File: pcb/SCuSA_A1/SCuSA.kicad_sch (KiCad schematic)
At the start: 37 parts, among them J102 USB4135-GF-A, J105 JST_S2B-PH-K-x, Q102 DMN2041LSD, SW101 SW_DPDT_x2, SW102 SW_SPST, U1 LM27762, U101 MCP73812T-420I-OT, U102 AD8418, U103 BQ297xy, U104 TLV803EA30DBZR

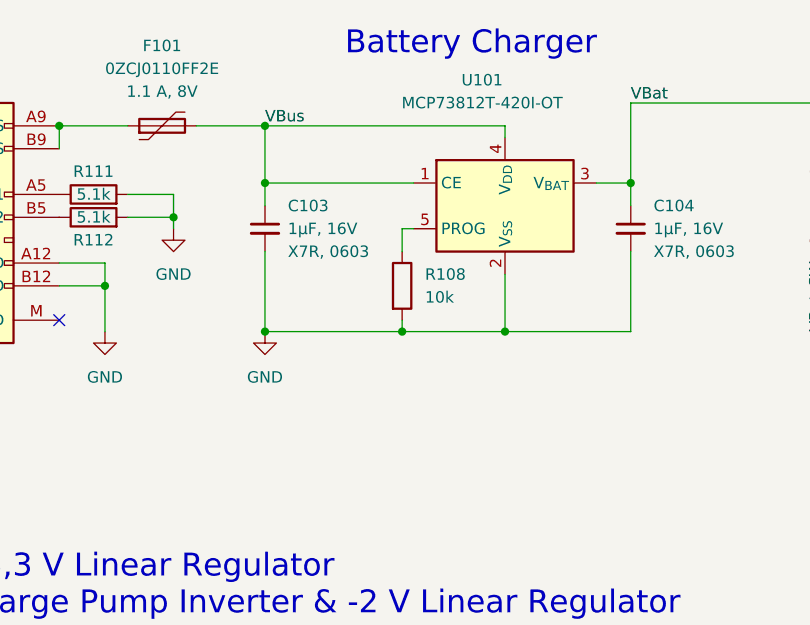
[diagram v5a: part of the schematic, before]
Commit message: Change battery charger
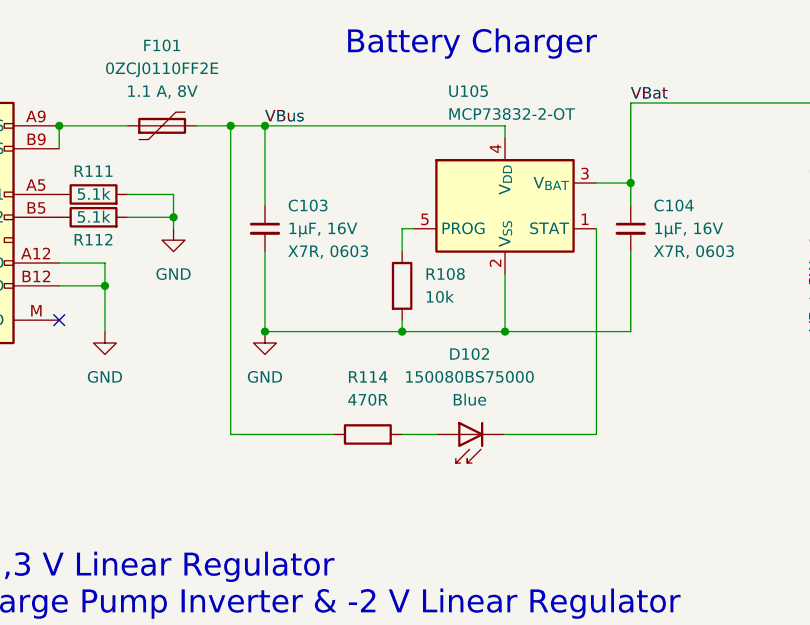
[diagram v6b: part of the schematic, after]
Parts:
- removed U101: MCP73812T-420I-OT, Package_TO_SOT_SMD:SOT-23-5, symbol Battery_Management:MCP73812T-420I-OT
- added D102: 150080BS75000, LED_SMD:LED_0805_2012Metric_Pad1.15x1.40mm_HandSolder, symbol LED_User:150080BS75000
- added R114: 470R,0603, Resistor_SMD:R_0603_1608Metric_Pad0.98x0.95mm_HandSolder, symbol Resistor_User:470R,0603
- added U105: MCP73832-2-OT, Package_TO_SOT_SMD:SOT-23-5, symbol Battery_Management:MCP73832-2-OT
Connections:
- net GND: now also U105.2 (V_{SS})
- net VBat: now also U105.3 (V_{BAT})
- net VBus: now also R114.1, U105.4 (V_{DD})
- net at R108.1: now also U105.5 (PROG)
- new net: D102.2 (A), R114.2
- new net: D102.1 (K), U105.1 (STAT)
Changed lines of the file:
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@@
   (junction (at 52.07 45.72) (diameter 0) (color 0 0 0 0)
   )
-  (junction (at 69.85 34.29) (diameter 0) (color 0 0 0 0)
-  )
   (junction (at 96.52 50.8) (diameter 0) (color 0 0 0 0)
   )
@@
   )
   (junction (at 236.22 27.94) (diameter 0) (color 0 0 0 0)
+  )
+  (junction (at 66.04 27.94) (diameter 0) (color 0 0 0 0)
   )
   (no_connect (at 46.99 49.53))
@@
     (stroke (width 0) (type default))
   )
-  (wire (pts (xy 69.85 36.83) (xy 69.85 34.29))
+  (wire (pts (xy 69.85 27.94) (xy 69.85 36.83))
     (stroke (width 0) (type default))
   )
@@
     (stroke (width 0) (type default))
   )
+  (wire (pts (xy 106.68 62.23) (xy 96.52 62.23))
+    (stroke (width 0) (type default))
+  )
   (wire (pts (xy 171.45 91.44) (xy 171.45 93.98))
     (stroke (width 0) (type default))
@@
     (stroke (width 0) (type default))
   )
-  (wire (pts (xy 96.52 29.21) (xy 96.52 27.94))
-    (stroke (width 0) (type default))
-  )
   (wire (pts (xy 236.22 41.91) (xy 236.22 38.1))
     (stroke (width 0) (type default))
@@
     (stroke (width 0) (type default))
   )
-  (wire (pts (xy 69.85 27.94) (xy 69.85 34.29))
-    (stroke (width 0) (type default))
-  )
   (wire (pts (xy 48.26 113.03) (xy 57.15 113.03))
     (stroke (width 0) (type default))
@@
     (stroke (width 0) (type default))
   )
+  (wire (pts (xy 106.68 39.37) (xy 106.68 62.23))
+    (stroke (width 0) (type default))
+  )
   (wire (pts (xy 251.46 52.07) (xy 236.22 52.07))
     (stroke (width 0) (type default))
@@
     (stroke (width 0) (type default))
   )
+  (wire (pts (xy 66.04 27.94) (xy 69.85 27.94))
+    (stroke (width 0) (type default))
+  )
   (wire (pts (xy 241.3 113.03) (xy 241.3 135.89))
     (stroke (width 0) (type default))
@@
     (stroke (width 0) (type default))
   )
+  (wire (pts (xy 96.52 27.94) (xy 96.52 29.21))
+    (stroke (width 0) (type default))
+  )
   (wire (pts (xy 69.85 50.8) (xy 85.09 50.8))
     (stroke (width 0) (type default))
@@
     (stroke (width 0) (type default))
   )
-  (wire (pts (xy 62.23 27.94) (xy 69.85 27.94))
+  (wire (pts (xy 62.23 27.94) (xy 66.04 27.94))
     (stroke (width 0) (type default))
   )
@@
     (stroke (width 0) (type default))
   )
+  (wire (pts (xy 66.04 62.23) (xy 66.04 27.94))
+    (stroke (width 0) (type default))
+  )
   (wire (pts (xy 190.5 43.18) (xy 190.5 44.45))
     (stroke (width 0) (type default))
@@
     (stroke (width 0) (type default))
   )
+  (wire (pts (xy 77.47 62.23) (xy 66.04 62.23))
+    (stroke (width 0) (type default))
+  )
   (wire (pts (xy 251.46 30.48) (xy 251.46 52.07))
     (stroke (width 0) (type default))
@@
     (stroke (width 0) (type default))
   )
-  (wire (pts (xy 69.85 34.29) (xy 86.36 34.29))
-    (stroke (width 0) (type default))
-  )
   (wire (pts (xy 90.17 135.89) (xy 90.17 138.43))
     (stroke (width 0) (type default))
   )
   (wire (pts (xy 106.68 34.29) (xy 110.49 34.29))
+    (stroke (width 0) (type default))
+  )
+  (wire (pts (xy 88.9 62.23) (xy 85.09 62.23))
     (stroke (width 0) (type default))
   )
@@
     )
   )
-  (symbol (lib_id "Battery_Management:MCP73812T-420I-OT") (at 96.52 36.83 0) (unit 1)
-    (in_bom yes) (on_board yes) (dnp no)
-    (property "Reference" "U101" (at 93.98 22.86 0)
-      (effects (font (size 1.27 1.27)))
-    )
-    (property "Value" "MCP73812T-420I-OT" (at 93.98 25.4 0)
-      (effects (font (size 1.27 1.27)))
-    )
-    (property "Footprint" "Package_TO_SOT_SMD:SOT-23-5" (at 97.79 43.18 0)
-      (effects (font (size 1.27 1.27)) (justify left) hide)
-    )
-    (property "Datasheet" "http://ww1.microchip.com/downloads/en/DeviceDoc/22036b.pdf" (at 90.17 30.48 0)
-      (effects (font (size 1.27 1.27)) hide)
-    )
-    (pin "1")
-    (pin "2")
-    (pin "3")
-    (pin "4")
-    (pin "5")
-    (instances
-      (project "SCuSA"
-        (path "/7c524ebf-103a-4dc7-9ca9-e5a941b364b9"
-          (reference "U101") (unit 1)
-        )
-      )
-    )
-  )
   (symbol (lib_id "Switch:SW_DPDT_x2") (at 241.3 140.97 270) (unit 2)
     (in_bom yes) (on_board yes) (dnp no) (fields_autoplaced)
@@
         (path "/7c524ebf-103a-4dc7-9ca9-e5a941b364b9"
           (reference "JP102") (unit 1)
+        )
+      )
+    )
+  )
+  (symbol (lib_id "Resistor_User:470R,0603") (at 81.28 62.23 90) (unit 1)
+    (in_bom yes) (on_board yes) (dnp no) (fields_autoplaced)
+    (property "Reference" "R114" (at 81.28 55.88 90)
+      (effects (font (size 1.27 1.27)))
+    )
+    (property "Value" "470R,0603" (at 78.74 60.325 0)
+      (effects (font (size 1.27 1.27)) (justify left) hide)
+    )
+    (property "Footprint" "Resistor_SMD:R_0603_1608Metric_Pad0.98x0.95mm_HandSolder" (at 91.44 59.69 0)
+      (effects (font (size 1.27 1.27)) hide)
+    )
+    (property "Datasheet" "~" (at 85.725 59.69 0)
+      (effects (font (size 1.27 1.27)) hide)
+    )
+    (property "Resistance" "470R" (at 81.28 58.42 90)
+      (effects (font (size 1.27 1.27)))
+    )
+    (property "Tolerance" "1%" (at 81.28 57.15 0)
+      (effects (font (size 1.27 1.27)) (justify left) hide)
+    )
+    (property "Power" "0.1W" (at 81.28 51.435 0)
+      (effects (font (size 1.27 1.27)) hide)
+    )
+    (property "Package" "0603" (at 83.82 57.785 0)
+      (effects (font (size 1.27 1.27)) hide)
+    )
+    (pin "1")
+    (pin "2")
+    (instances
+      (project "SCuSA"
+        (path "/7c524ebf-103a-4dc7-9ca9-e5a941b364b9"
+          (reference "R114") (unit 1)
         )
       )
@@
     )
   )
+  (symbol (lib_id "LED_User:150080BS75000") (at 91.44 62.23 180) (unit 1)
+    (in_bom yes) (on_board yes) (dnp no) (fields_autoplaced)
+    (property "Reference" "D102" (at 92.583 53.34 0)
+      (effects (font (size 1.27 1.27)))
+    )
+    (property "Value" "150080BS75000" (at 92.583 55.88 0)
+      (effects (font (size 1.27 1.27)))
+    )
+    (property "Footprint" "LED_SMD:LED_0805_2012Metric_Pad1.15x1.40mm_HandSolder" (at 91.44 66.675 0)
+      (effects (font (size 1.27 1.27)) hide)
+    )
+    (property "Datasheet" "https://www.we-online.com/katalog/datasheet/150080BS75000.pdf" (at 92.71 62.23 0)
+      (effects (font (size 1.27 1.27)) hide)
+    )
+    (property "Manufacturer" "Wurth Elektronik" (at 104.14 54.61 0)
+      (effects (font (size 1.27 1.27)) (justify left) hide)
+    )
+    (property "Supplier" "Digi-Key" (at 104.14 52.07 0)
+      (effects (font (size 1.27 1.27)) (justify left) hide)
+    )
+    (property "SPN" "732-4982-1-ND" (at 93.98 52.07 0)
+      (effects (font (size 1.27 1.27)) (justify left) hide)
+    )
+    (property "Info" "Blue" (at 92.583 58.42 0)
+      (effects (font (size 1.27 1.27)))
+    )
+    (pin "1")
+    (pin "2")
+    (instances
+      (project "SCuSA"
+        (path "/7c524ebf-103a-4dc7-9ca9-e5a941b364b9"
+          (reference "D102") (unit 1)
+        )
+      )
+    )
+  )
   (symbol (lib_id "Resistor_User:120k,0603") (at 90.17 109.22 0) (unit 1)
     (in_bom yes) (on_board yes) (dnp no) (fields_autoplaced)
@@
         )
       )
+    )
+  )
+  (symbol (lib_id "Battery_Management:MCP73832-2-OT") (at 96.52 36.83 0) (unit 1)
+    (in_bom yes) (on_board yes) (dnp no)
+    (property "Reference" "U105" (at 90.17 24.13 0)
+      (effects (font (size 1.27 1.27)) (justify left))
+    )
+    (property "Value" "MCP73832-2-OT" (at 90.17 26.67 0)
+      (effects (font (size 1.27 1.27)) (justify left))
+    )
+    (property "Footprint" "Package_TO_SOT_SMD:SOT-23-5" (at 97.79 43.18 0)
+      (effects (font (size 1.27 1.27) italic) (justify left) hide)
+    )
+    (property "Datasheet" "http://ww1.microchip.com/downloads/en/DeviceDoc/20001984g.pdf" (at 92.71 38.1 0)
+      (effects (font (size 1.27 1.27)) hide)
+    )
+    (pin "1")
+    (pin "2")
+    (pin "3")
+    (pin "4")
+    (pin "5")
+    (instances
+      (project "SCuSA"
+        (path "/7c524ebf-103a-4dc7-9ca9-e5a941b364b9"
+          (reference "U105") (unit 1)
+        )
+      )

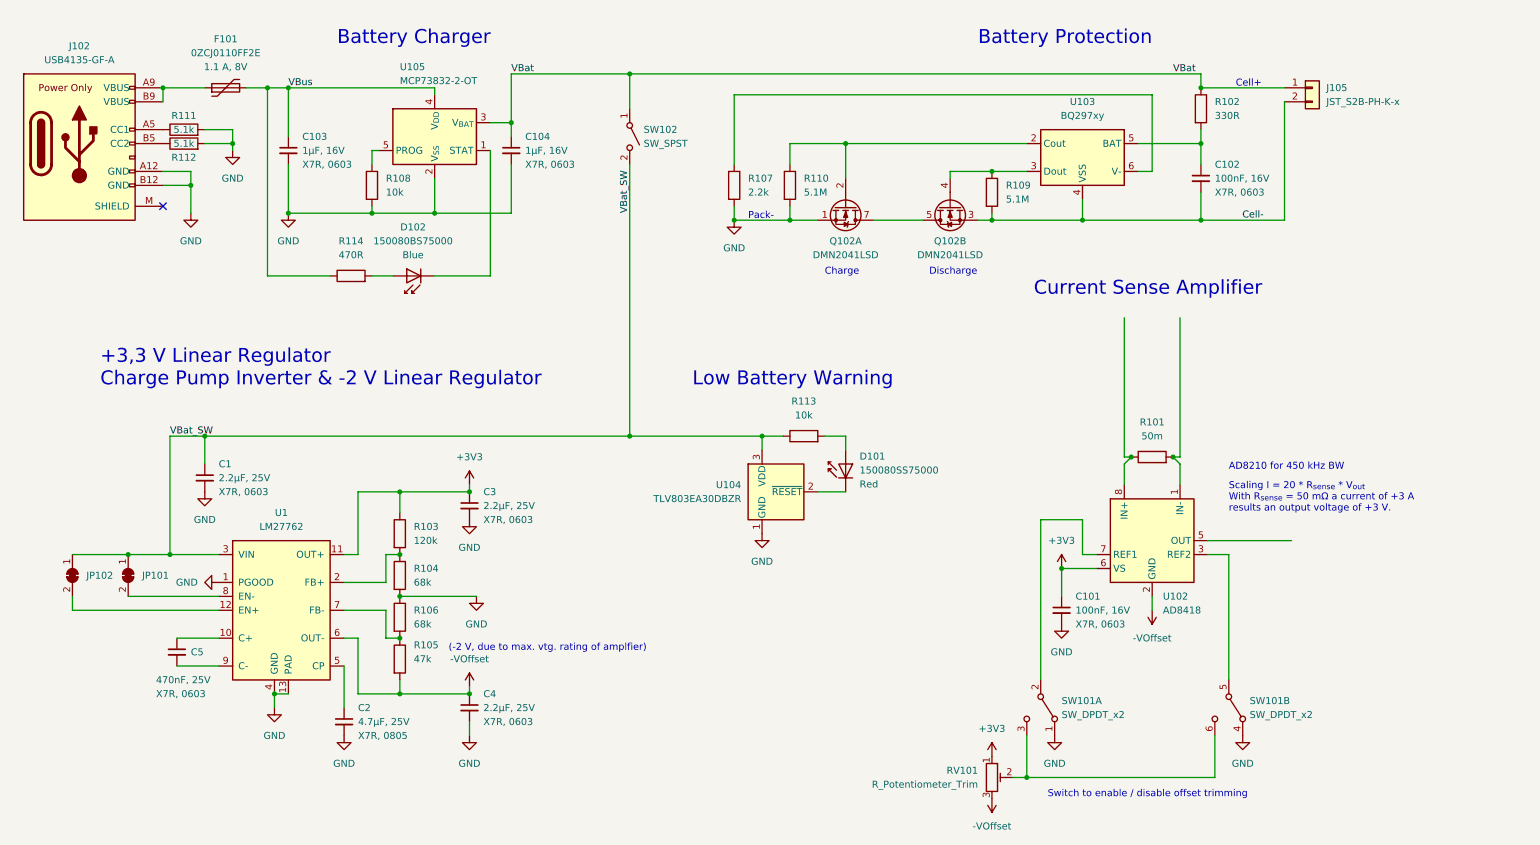
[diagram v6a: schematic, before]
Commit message: Add trimpot, bindingpost
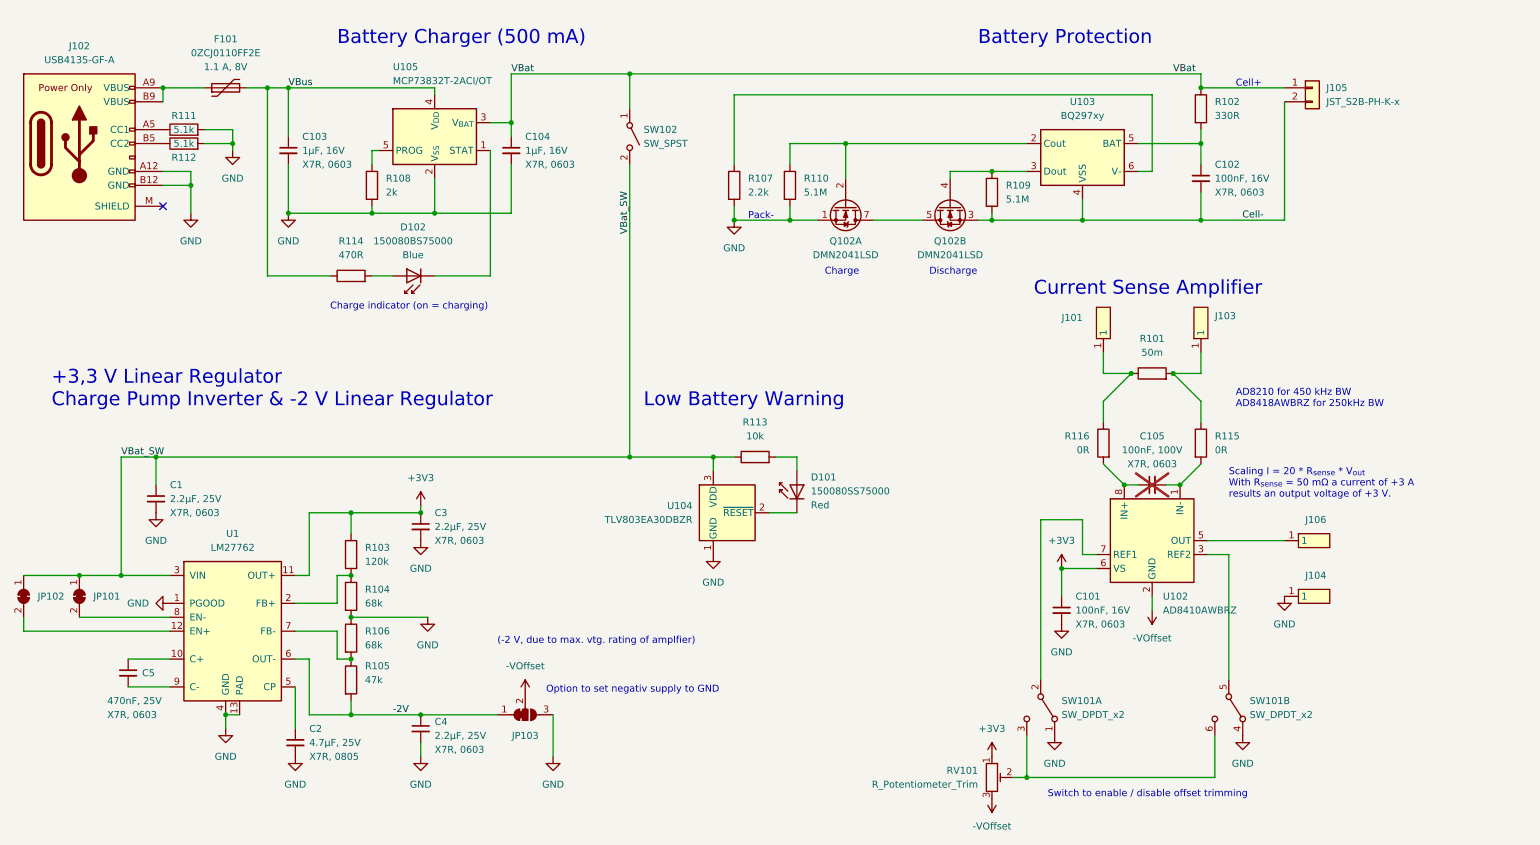
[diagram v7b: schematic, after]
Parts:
- removed R108: 10k,0603, Resistor_SMD:R_0603_1608Metric_Pad0.98x0.95mm_HandSolder, symbol Resistor_User:10k,0603
- added C105: 100nF,100V,X7R,0603, Capacitor_SMD:C_0603_1608Metric_Pad1.08x0.95mm_HandSolder, symbol Capacitor_User:100nF,100V,X7R,0603
- added J101, J106: Binding_Post_PK4_Red, Connector_User:Binding_Post_4.3mm_M4_DIN965_Pad, symbol Connector_User:Binding_Post_PK4_Red
- added J103, J104: Binding_Post_PK4_Black, Connector_User:Binding_Post_4.3mm_M4_DIN965_Pad, symbol Connector_User:Binding_Post_PK4_Black
- added JP103: SolderJumper_3_Bridged12, symbol Jumper:SolderJumper_3_Bridged12
- added R108: 2k,0603, Resistor_SMD:R_0603_1608Metric_Pad0.98x0.95mm_HandSolder, symbol Resistor_User:2k,0603
- added R115, R116: 0R,0603, Resistor_SMD:R_0603_1608Metric_Pad0.98x0.95mm_HandSolder, symbol Resistor_User:0R,0603
- U102: value AD8418 -> AD8410AWBRZ; footprint (none) -> Package_SO:SOIC-8_3.9x4.9mm_P1.27mm; SPN (none) -> 505-AD8410AWBRZ-ND; Supplier (none) -> Digi-Key
- U105: value MCP73832-2-OT -> MCP73832T-2ACI/OT; SPN (none) -> MCP73832T-2ACI/OTCT-ND; Supplier (none) -> Digi-Key
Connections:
- net GND: now also J104.1, JP103.3 (B), R108.2
- net at U102.1 (IN-): now also C105.2, R115.2; no longer R101.2
- net at U102.5 (OUT): now also J106.1
- net at U102.8 (IN+): now also C105.1, R116.2; no longer R101.1
- net at U105.5 (PROG): now also R108.1
- net -2V: now reaches C4.1, R105.2, U1.6 (OUT-)
- net -2V: now also JP103.1 (A)
- new net: J103.1, R101.2, R115.1
- new net: J101.1, R101.1, R116.1
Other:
- note added: "AD8210 for 450 kHz BW AD8418AWBRZ for 250kHz BW"
- note added: "Battery Charger (500 mA)"
- note added: "Charge indicator (on = charging)"
- note added: "Option to set negativ supply to GND"
- note removed: "AD8210 for 450 kHz BW"
- note removed: "Battery Charger"
- moved on the sheet: C1, C2, C3, C4, C5, D101, JP101, JP102, R101, R103, R104, R105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

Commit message: Completion of schematic (for now)
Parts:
- removed SW101: SW_DPDT_x2, symbol Switch:SW_DPDT_x2
- removed SW102: SW_SPST, symbol Switch:SW_SPST
- added C109, C111: 100nF,100V,X7R,0603, Capacitor_SMD:C_0603_1608Metric_Pad1.08x0.95mm_HandSolder, symbol Capacitor_User:100nF,100V,X7R,0603
- added D103: 150080SS75000, LED_SMD:LED_0805_2012Metric_Pad1.15x1.40mm_HandSolder, symbol LED_User:150080SS75000
- added R117: 10k,0603, Resistor_SMD:R_0603_1608Metric_Pad0.98x0.95mm_HandSolder, symbol Resistor_User:10k,0603
- added SW101, SW102: JS202011CQN, Button_Switch_THT:SW_CuK_JS202011CQN_DPDT_Straight, symbol Switch_User:Slide_Switch_JS202011CQN
- JP101: renamed from JP102; footprint (none) -> Jumper:SolderJumper-2_P1.3mm_Bridged_Pad1.0x1.5mm
- JP102: renamed from JP101; footprint (none) -> Jumper:SolderJumper-2_P1.3mm_Bridged_Pad1.0x1.5mm
- JP103: footprint (none) -> Jumper:SolderJumper-3_P1.3mm_Bridged12_Pad1.0x1.5mm_NumberLabels
- R114: renamed from R101; footprint (none) -> Resistor_SMD:R_1206_3216Metric; symbol Device:R -> Resistor_User:50m,1206; Package (none) -> 1206; Power (none) -> 1W; Resistance (none) -> 50m; Tolerance (none) -> 0.5%
- RV101: value R_Potentiometer_Trim -> 10k_Potentiometer_Trim_TSR-3296W; footprint (none) -> Potentionmeter_THT_User:Potentiometer_Suntan_3296W_Vertical; symbol Device:R_Potentiometer_Trim -> Resistor_User:10k_Potentiometer_Trim_TSR-3296W; MPN (none) -> TSR-3296W; Manufacturer (none) -> Suntan; SPN (none) -> 64W-10K; Supplier (none) -> Reichelt
- renumbered C103 to C101, C104 to C102, C102 to C103, C1 to C104, C3 to C105, C5 to C106, C4 to C107, C2 to C108, C105 to C110, C101 to C112, D102 to D101, D101 to D102, J102 to J101, J105 to J102, J101 to J103, J103 to J104, J106 to J105, J104 to J106, Q102 to Q101, R111 to R101, R112 to R102, R108 to R103, R114 to R104, R102 to R105, R107 to R106, R110 to R107, R109 to R108, R113 to R109, R103 to R110, R104 to R111, R106 to R112, R105 to R113, R116 to R115, R115 to R116, U105 to U101, U103 to U102, U104 to U103, U1 to U104, U102 to U105
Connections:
- net GND: now also C109.1, C111.2, D103.1 (K), SW102.1 (A), SW102.4 (A); no longer U104.1 (PGOOD)
- net VBat: now also SW101.1 (A), SW101.4 (A)
- net VBat_SW: now also R117.2, SW101.2 (B), SW101.5 (B)
- net at C110.2, R116.2, U105.1 (IN-): now also C111.1
- net -VOffset: now reaches U105.2 (GND)
- net -VOffset: now also JP103.2 (C), RV101.3
- net at U105.3 (REF2): now also SW102.5 (B)
- net at U105.7 (REF1): now also SW102.2 (B)
- net at C110.1, R115.2, U105.8 (IN+): now also C109.2
- net at RV101.2: now also SW102.3 (C), SW102.6 (C)
- new net PGOOD: D103.2 (A), R117.1, U104.1 (PGOOD)
- no-connect marks 1 -> 3
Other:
- note added: "(Cell+)"
- note added: "(Pack-)"
- note added: "Power Fail LED"
- note removed: "Cell+"
- note removed: "Pack-"
- moved on the sheet: C104, C105, C106, C107, C108, F101, J105, J106, JP101, JP102, JP103, Q101A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
